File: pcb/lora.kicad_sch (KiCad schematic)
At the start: 91 parts, among them J1 Conn_01x04, J11 Conn_Coaxial, J2 5V, J3 Conn_01x06, J4 USB_C_Receptacle_USB2.0, J5 Temp, J6 VDD, J7 UART, J8 Conn_01x04, Q1 AO3401A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

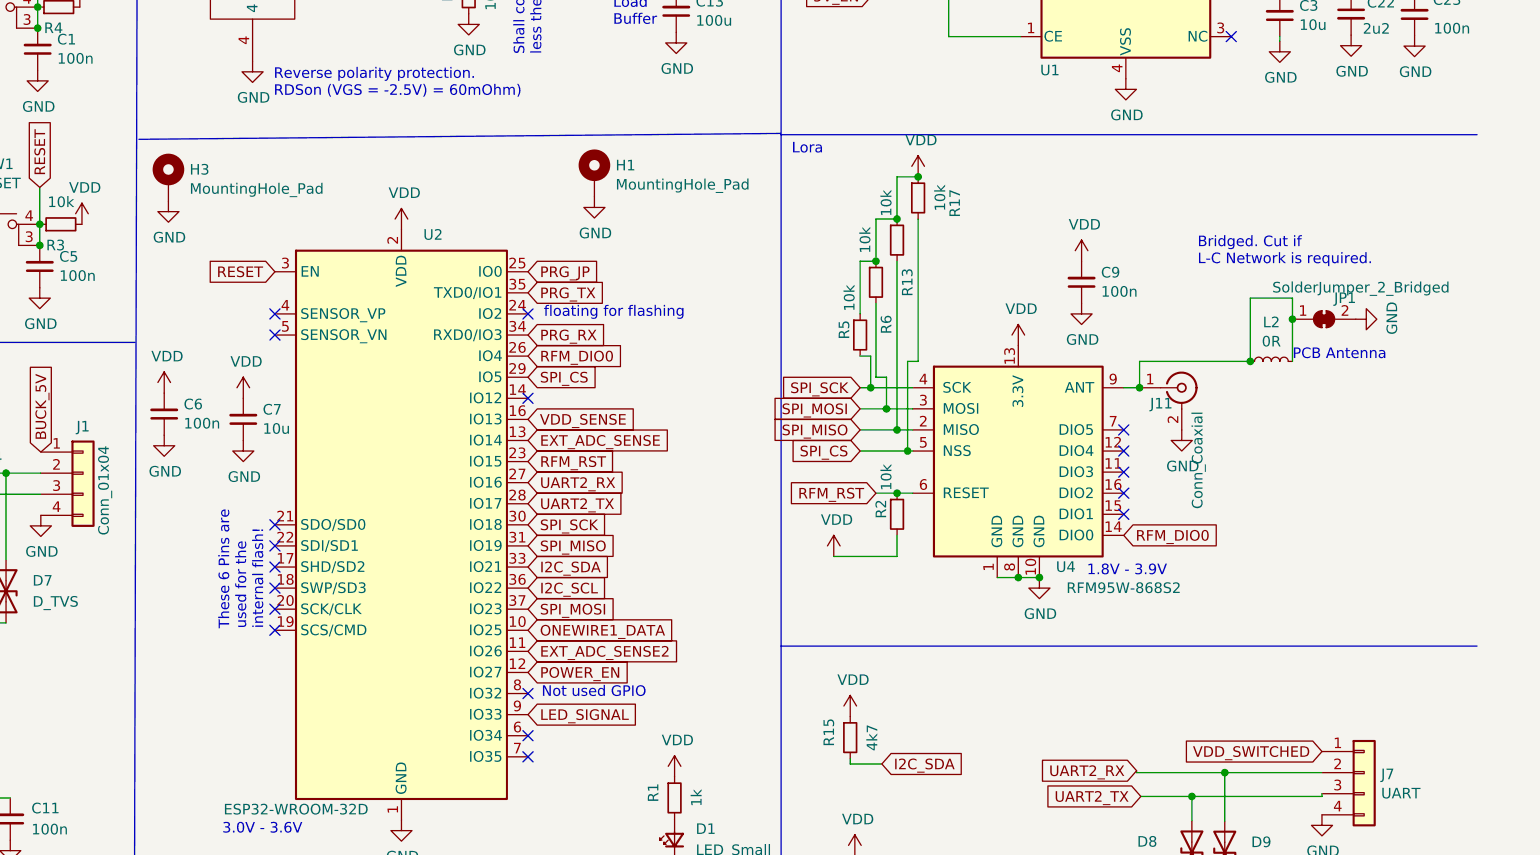
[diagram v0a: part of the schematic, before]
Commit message: added spi header and connected dio1 of rfm95
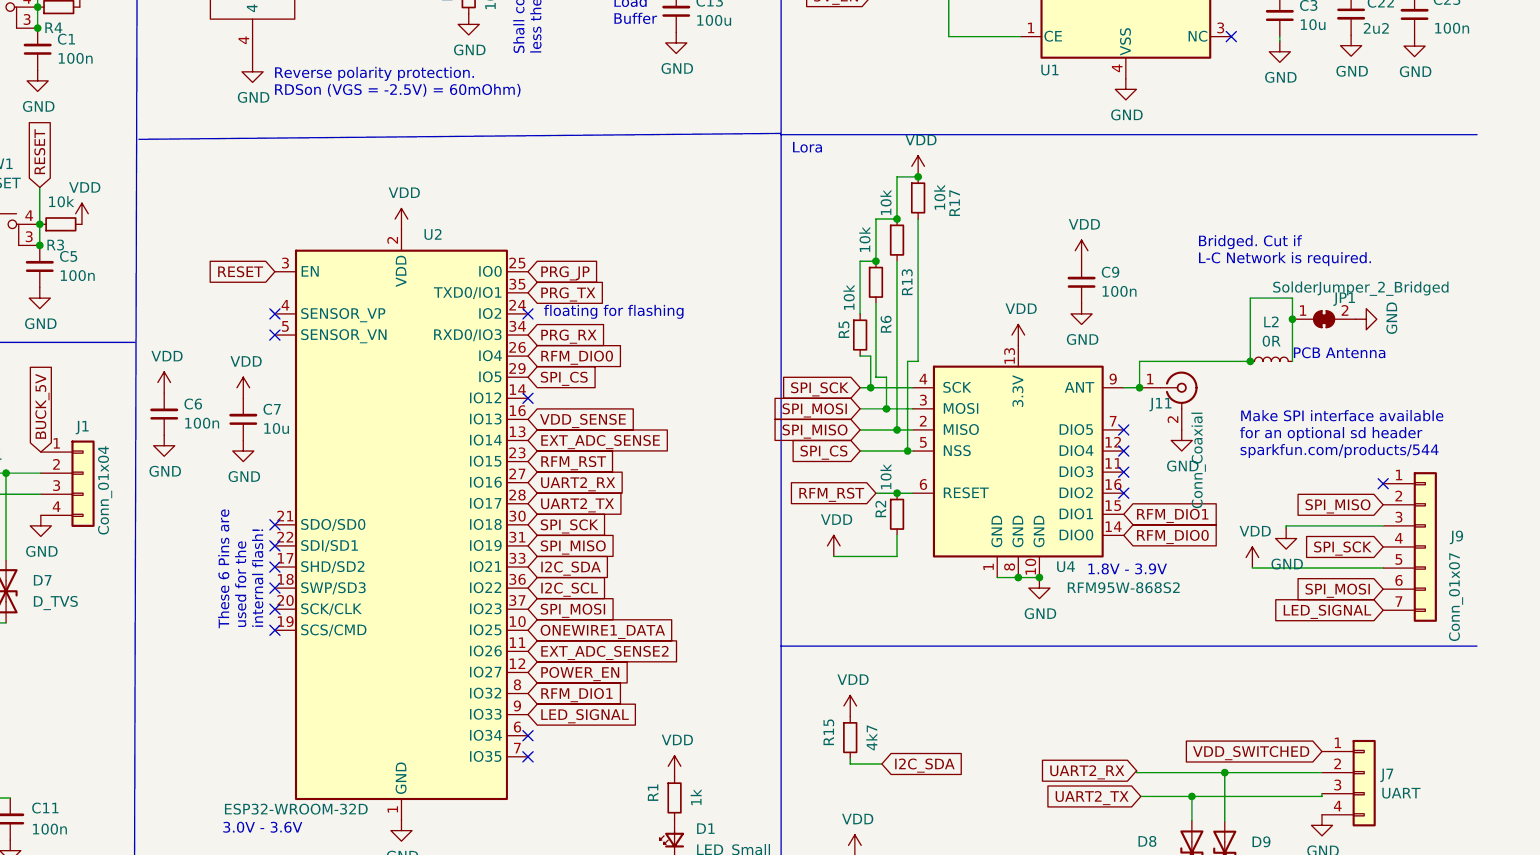
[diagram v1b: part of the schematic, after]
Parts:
- removed H1, H3: MountingHole_Pad, MountingHole:MountingHole_2.2mm_M2_DIN965_Pad, symbol Mechanical:MountingHole_Pad
- added J9: Conn_01x07, Connector_PinHeader_2.54mm:PinHeader_1x07_P2.54mm_Vertical, symbol Connector_Generic:Conn_01x07
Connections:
- net GND: now also J9.3 (Pin_3)
- net LED_SIGNAL: now also J9.7 (Pin_7)
- net SPI_MISO: now also J9.2 (Pin_2)
- net SPI_MOSI: now also J9.6 (Pin_6)
- net SPI_SCK: now also J9.4 (Pin_4)
- net VDD: now also J9.5 (Pin_5)
- net RFM_DIO1: now reaches U2.8 (IO32)
- net RFM_DIO1: now also U4.15 (DIO1)
- no-connect marks 24 -> 23
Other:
- note added: "Make SPI interface available for an optional sd header sparkfun.com/products/544"
- note removed: "Not used GPIO"

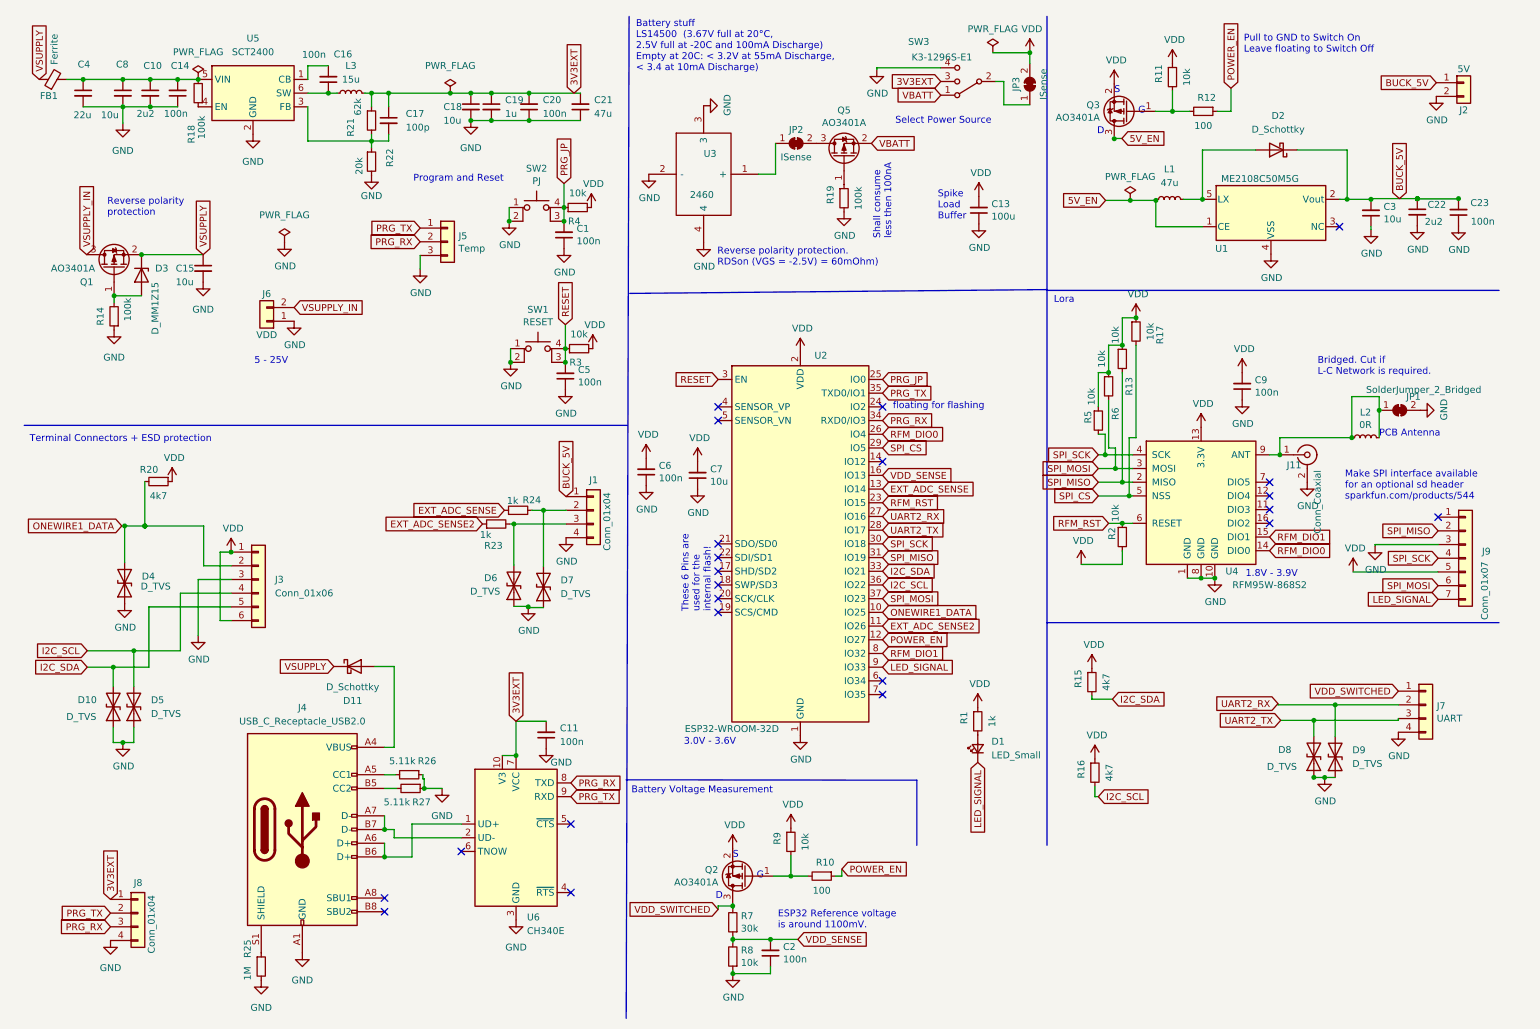
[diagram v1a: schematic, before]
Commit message: v2.2 finalized, spi connector added and ground current measurement solder jumper added
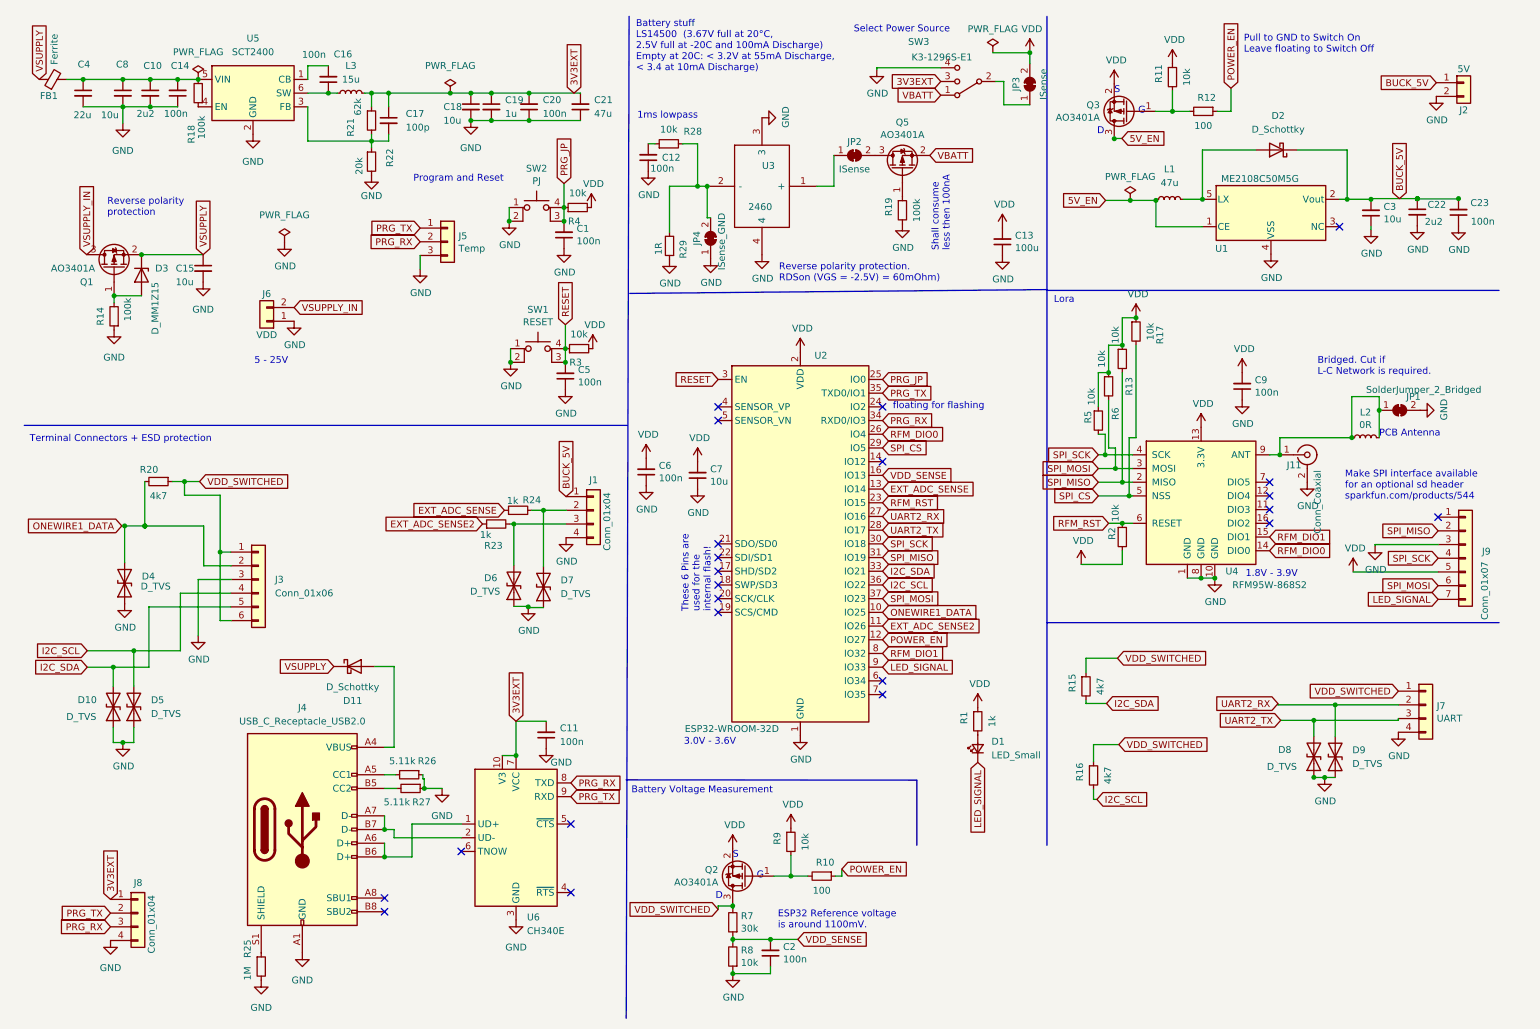
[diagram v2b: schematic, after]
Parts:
- added C12: 100n, Capacitor_SMD:C_0603_1608Metric, symbol Device:C_Small
- added JP4: ISense_GND, Jumper:SolderJumper-2_P1.3mm_Bridged_RoundedPad1.0x1.5mm, symbol Jumper:SolderJumper_2_Bridged
- added R28: 10k, Resistor_SMD:R_0603_1608Metric, symbol Device:R_Small
- added R29: 1R, Resistor_SMD:R_0603_1608Metric, symbol Device:R_Small
- C19: LCSC C15849 -> C90540
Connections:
- net GND: now also C12.1, JP4.1 (A), R29.1; no longer U3.2 (-)
- net VDD: no longer J3.1 (Pin_1), J3.6 (Pin_6), R15.1, R16.1, R20.1
- net VDD_SWITCHED: now also J3.1 (Pin_1), J3.6 (Pin_6), R15.1, R16.1, R20.1
- new net: JP4.2 (B), R28.2, R29.2, U3.2 (-)
- new net: C12.2, R28.1
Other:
- note added: "1ms lowpass"
- note removed: "Spike Load Buffer"
- moved on the sheet: C13, JP2, Q5, R15, R16, R19, U3
